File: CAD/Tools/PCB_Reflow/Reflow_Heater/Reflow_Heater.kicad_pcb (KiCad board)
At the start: 2 copper layers, 52.5 x 100 mm, 6 parts, among them J1 Screw Connector, J2 Screw_Connector

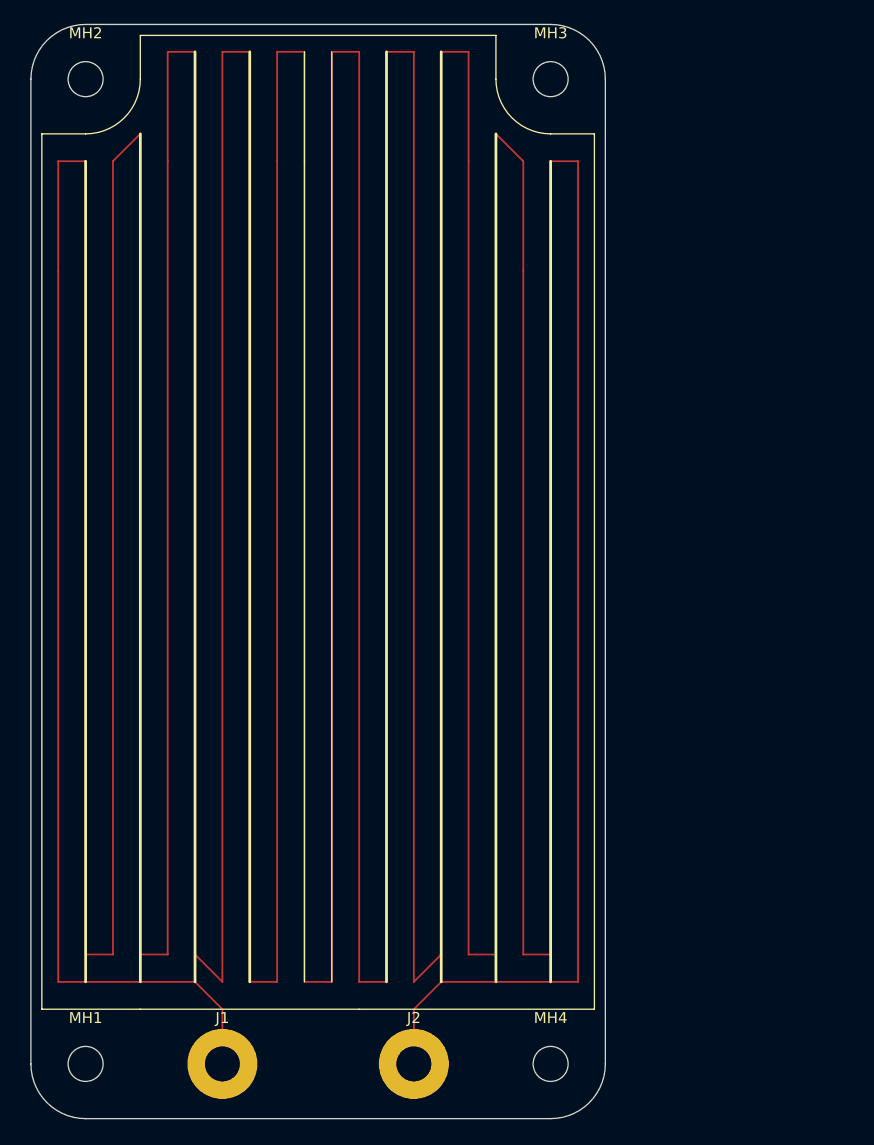
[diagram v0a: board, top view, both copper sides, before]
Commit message: feat: 100x75mm heater, pushing 3C/s rating
moving to smaller 100x50 mm heater, and then stacking 2 next to each other
if more space/power is needed.  I don't think it will though
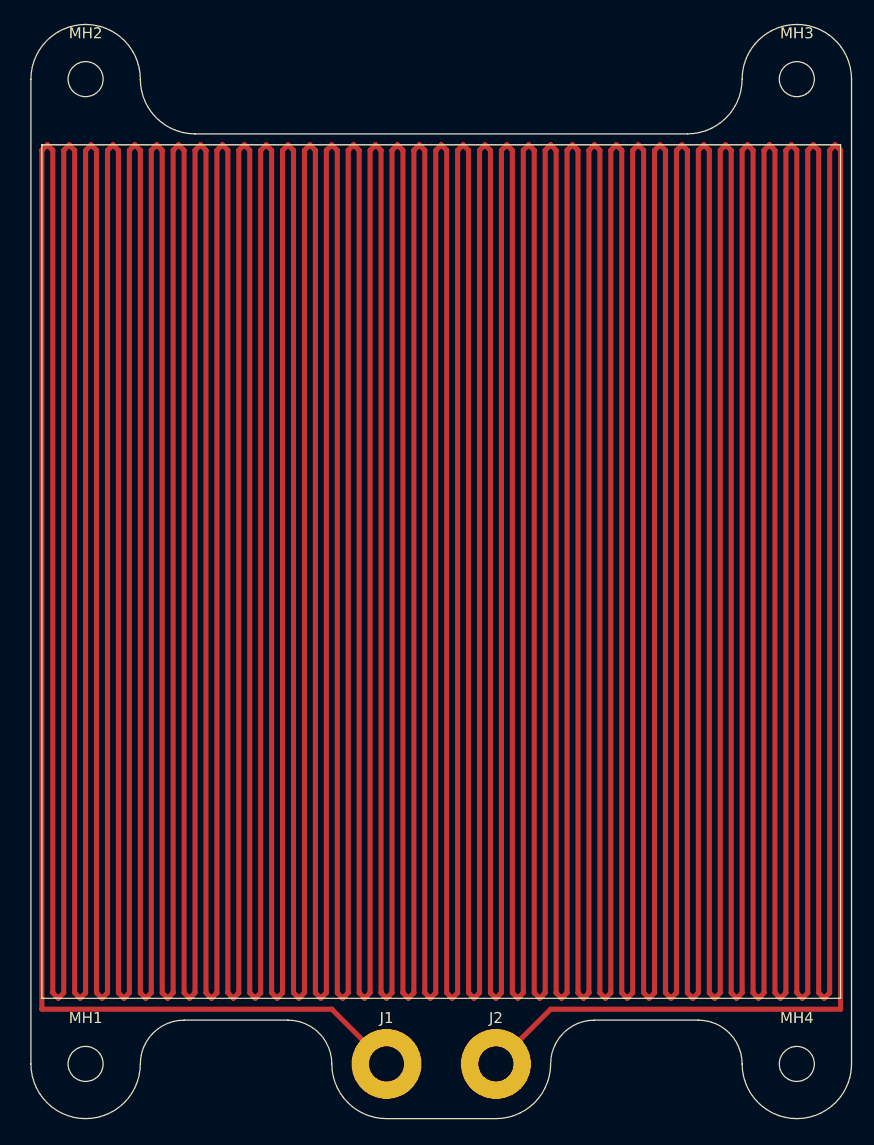
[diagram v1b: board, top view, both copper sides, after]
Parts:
- moved MH3 22.5 mm to (120.0, 70.0)
- moved MH4 22.5 mm to (120.0, 160.0)
- moved J1 15.0 mm to (82.5, 160.0)
- moved J2 7.50 mm to (92.5, 160.0)
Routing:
- net Net-(J1-Pad1): track 1693.7 -> 5871.4 mm
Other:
- board size 52.5 x 100 mm -> 75 x 100 mm

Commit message: feat: 100x50 (78x49 usable space) smaller heater & gerbers
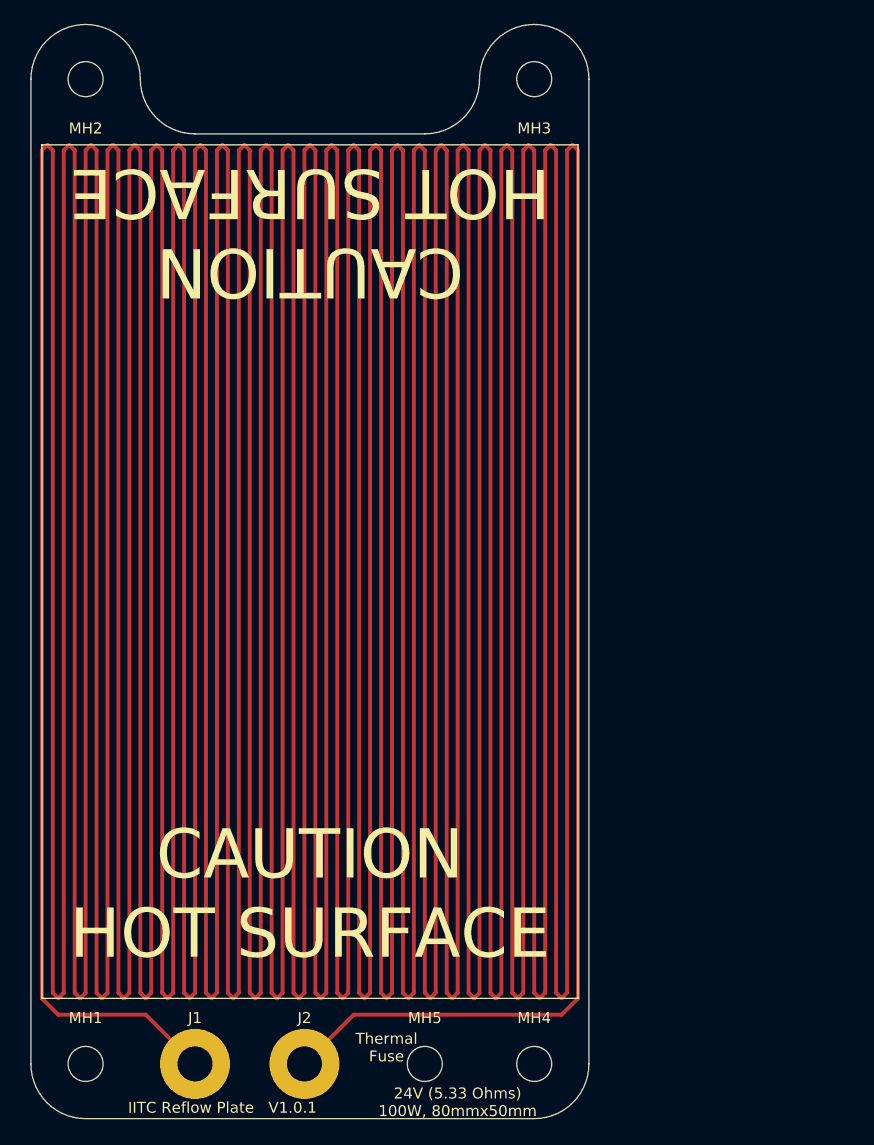
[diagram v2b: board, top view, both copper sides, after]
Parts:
- added MH5: ThermalFuse, Mounting_Holes:MountingHole_3.2mm_M3, F.Cu at (86.0, 160.0)
- moved MH3 24.0 mm to (96.0, 70.0)
- moved MH4 24.0 mm to (96.0, 160.0)
- moved J1 17.5 mm to (65.0, 160.0)
- moved J2 17.5 mm to (75.0, 160.0)
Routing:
- net Net-(J1-Pad1): track 5871.4 -> 3964.3 mm
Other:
- board size 75 x 100 mm -> 51 x 100 mm
- board text added: "24V (5.33 Ohms) 100W, 80mmx50mm"
- board text added: "CAUTION HOT SURFACE"
- board text added: "IITC Reflow Plate V1.0.1"
- board text added: "Thermal Fuse"

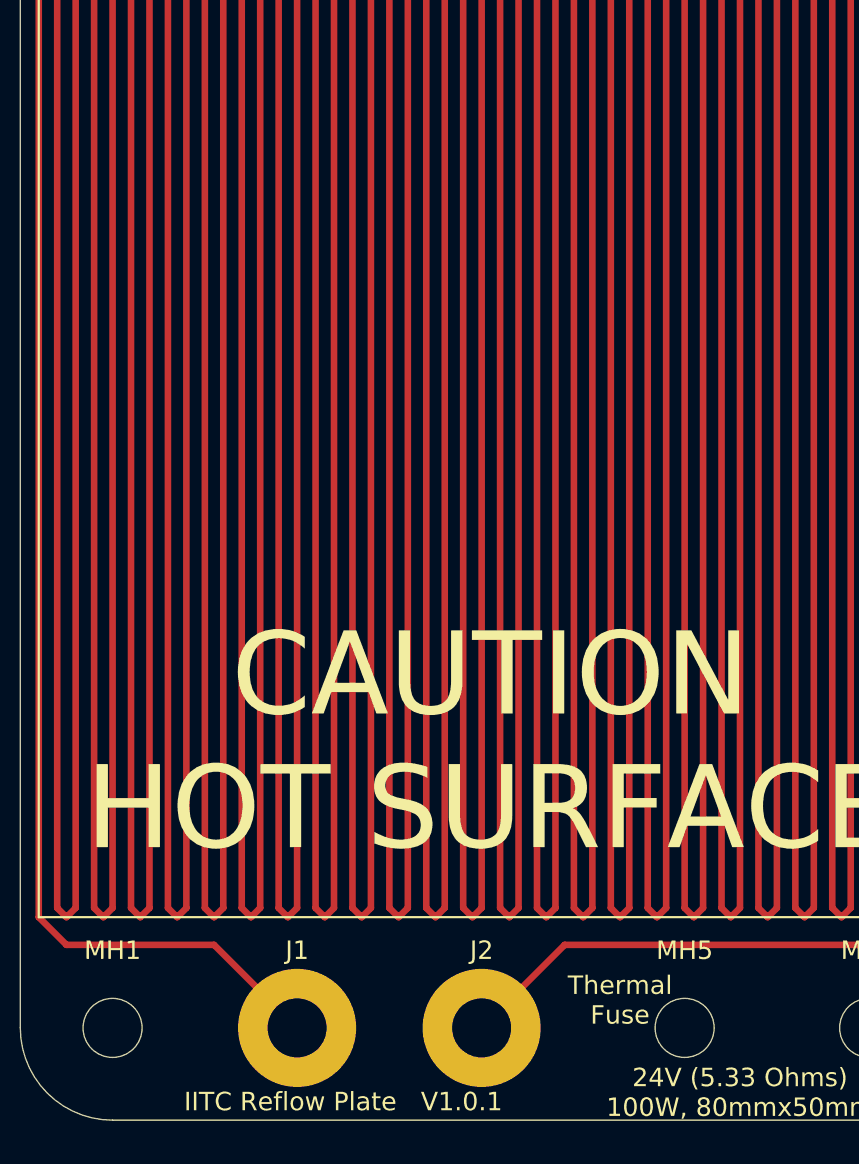
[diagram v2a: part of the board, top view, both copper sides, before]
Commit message: fix: silkscreen reversed, add hot surface graphic
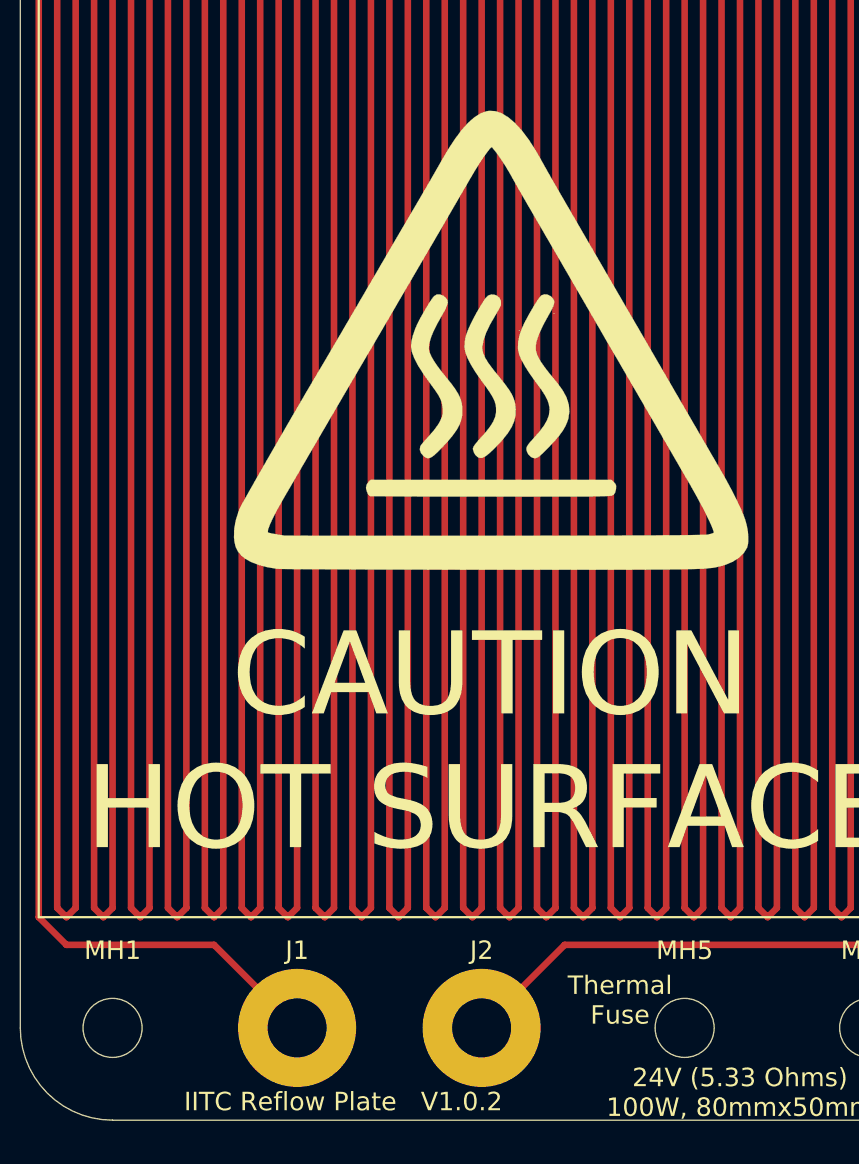
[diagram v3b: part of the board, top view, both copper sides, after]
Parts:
- added G***: LOGO, Warning-Graphics:Warning-HotSurface-30x30mm, B.Cu at (75.7, 105.6)
- added G***: LOGO, Warning-Graphics:Warning-HotSurface-30x30mm, F.Cu at (75.5, 122.9)
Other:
- board text added: "IITC Reflow Plate V1.0.2"
- board text removed: "IITC Reflow Plate V1.0.1"
